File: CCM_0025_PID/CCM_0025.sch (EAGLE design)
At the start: 110 parts, among them IC1 AD825, IC10 AD825, IC11 AD825, IC2 AD825, IC3 AD8226, IC4 AD8226, IC5 AD825, IC6 AD825, IC7 AD825, IC8 AD825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

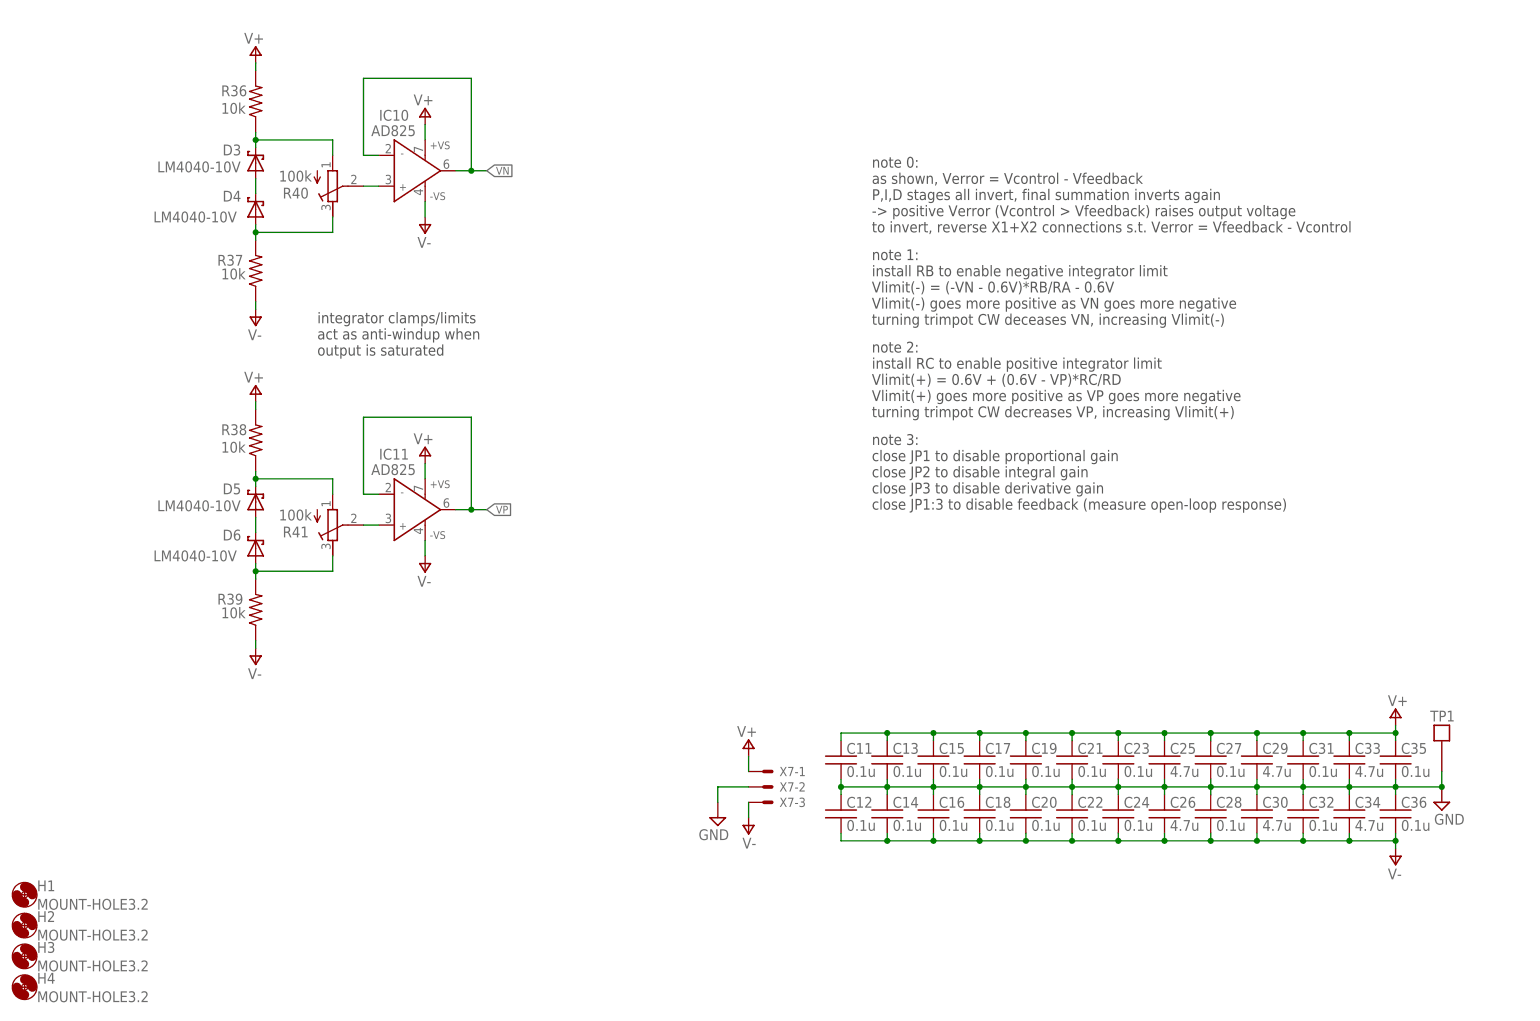
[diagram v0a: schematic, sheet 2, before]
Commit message: updates to schematic of CCM_0025, PID
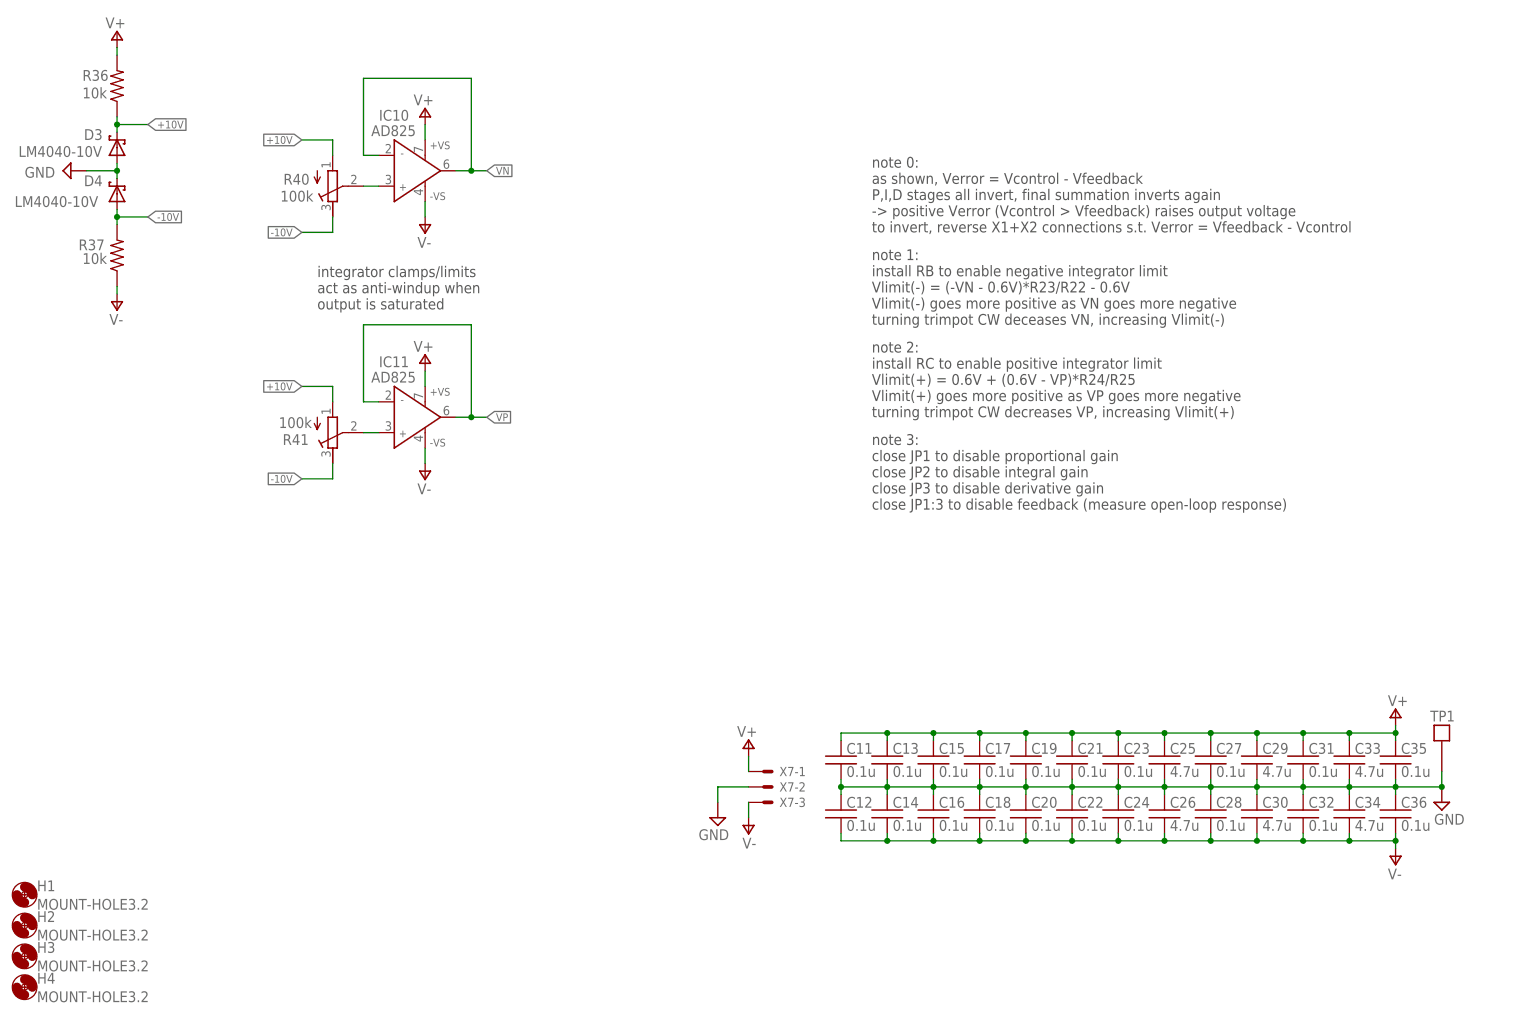
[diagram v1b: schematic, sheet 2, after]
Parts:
- removed D5, D6: LM4040-10V, noah:LM4040
- removed R38, R39: 10k, acrooptics:R0603
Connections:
- removed net N$22: D3.C, R36.1, R40.A
- removed net N$28: D3.A, D4.C
- removed net N$35: D5.C, R38.1, R41.A
- removed net N$40: D4.A, R37.2, R40.E
- removed net N$42: D5.A, D6.C
- removed net N$43: D6.A, R39.2, R41.E
- new net +10V: D3.C, R36.1, R40.A, R41.A
- new net -10V: D4.A, R37.2, R40.E, R41.E
- net GND: now also D3.A, D4.C
- net V+: no longer R38.2
- net V-: no longer R39.1
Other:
- note added: "note 1: install RB to enable negative integrator limit Vlimit(-) = (-VN - 0.6V)*R23/R22 - 0.6V Vlimit(-) goes more positive as VN goes more negative turning trimpot CW deceases VN, increasing Vlimit(-)"
- note added: "note 2: install RC to enable positive integrator limit Vlimit(+) = 0.6V + (0.6V - VP)*R24/R25 Vlimit(+) goes more positive as VP goes more negative turning trimpot CW decreases VP, increasing Vlimit(+)"
- note removed: "note 1: install RB to enable negative integrator limit Vlimit(-) = (-VN - 0.6V)*RB/RA - 0.6V Vlimit(-) goes more positive as VN goes more negative turning trimpot CW deceases VN, increasing Vlimit(-)"
- note removed: "note 2: install RC to enable positive integrator limit Vlimit(+) = 0.6V + (0.6V - VP)*RC/RD Vlimit(+) goes more positive as VP goes more negative turning trimpot CW decreases VP, increasing Vlimit(+)"
- moved on the sheet: D3, D4, IC11, R36, R37, R41
